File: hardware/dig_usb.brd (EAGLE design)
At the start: 146.1 x 102.6 mm, 175 parts, among them IC101 AT90USB1287-AU, IC102 74HC166D, IC103 MAX487CSA, IC202 DS1337S, IC301 LTV-356T, IC302 LTV-356T, IC303 LTV-356T, IC304 LTV-356T, IC305 LTV-356T, IC306 LTV-356T, IC307 LTV-356T, IC308 LTV-356T, K401 S202S02, K402 S202S02, K403 S202S02, K404 S202S02, K405 S202S02, K406 S202S02, K407 S202S02, K408 S202S02, Q1 16MHz, Q201 32,768kHz, T301 BCR191, T302 BCR191, T303 BCR191, T304 BCR191, T305 BCR191, T306 BCR191, T307 BCR191, T308 BCR191, X102 ISP, X301 RIA-73-02, X302 RIA-73-02, X303 RIA-73-02, X304 RIA-73-02, X305 RIA-73-02, X401 RIA-73-02, X402 RIA-73-02, X403 RIA-73-02, X404 RIA-73-02, X405 RIA-73-02, X406 RIA-73-02, X407 RIA-73-02

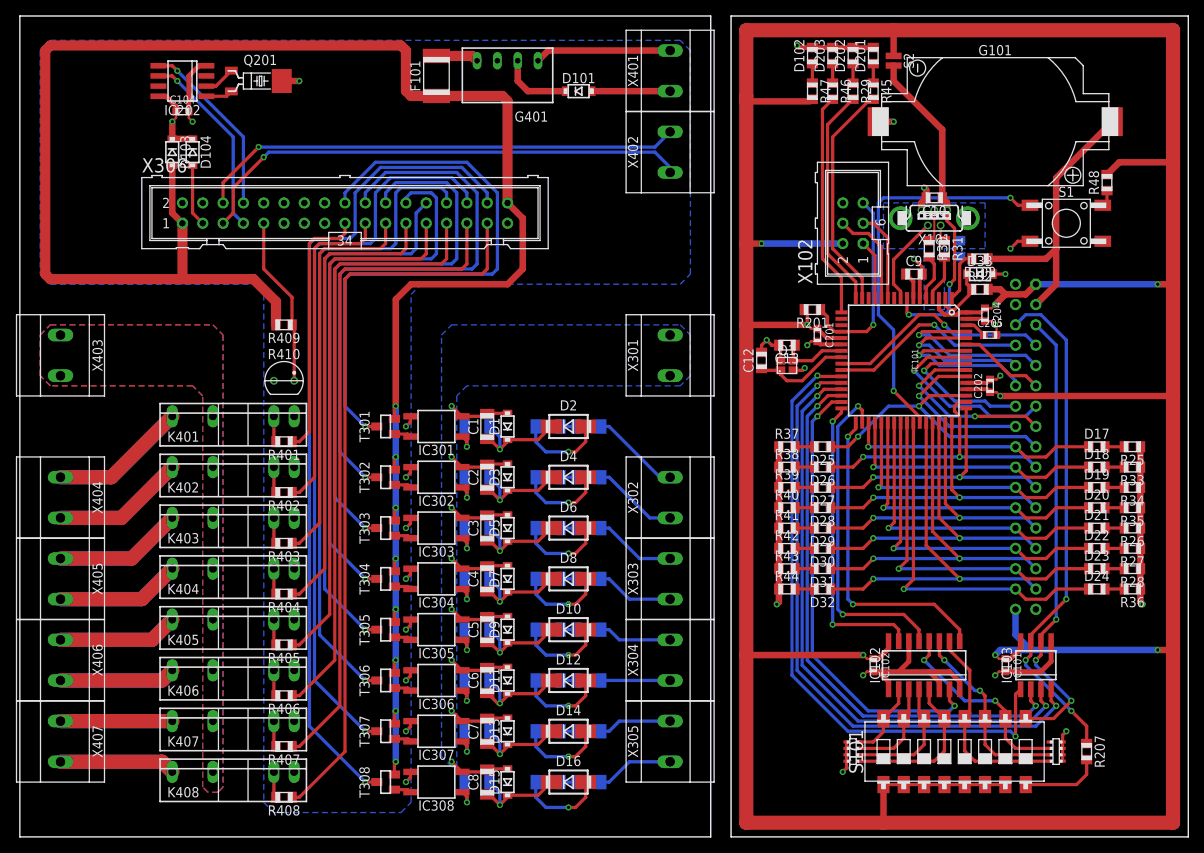
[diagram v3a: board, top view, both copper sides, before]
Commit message: Steckbare Anschlüsse zu dig_usb hinzugefügt
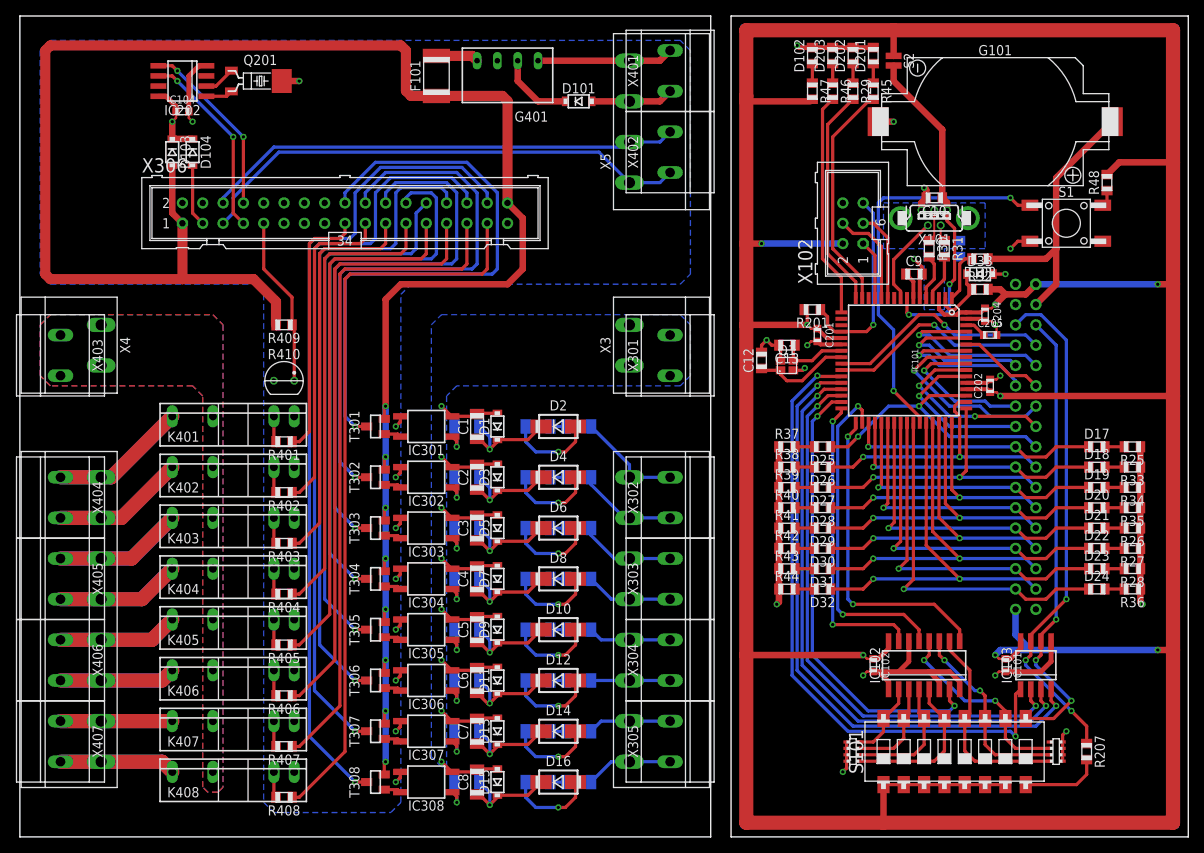
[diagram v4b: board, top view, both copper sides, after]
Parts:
- added X1, X2: AKL_249-08, anschluss:AKL_230-08
- added X3, X4: AKL_230-02, anschluss:AKL_230-02
- added X5: AKL_230-04, anschluss:AKL_230-04
- moved R1 1.27 mm to (64.8, 50.8)
- moved R10 1.27 mm to (64.8, 31.8)
- moved R11 1.27 mm to (69.8, 31.8)
- moved R13 1.27 mm to (64.8, 25.4)
- moved R14 1.27 mm to (69.8, 25.4)
- moved R16 1.27 mm to (64.8, 19.1)
- moved R17 1.27 mm to (69.8, 19.1)
- moved R19 1.27 mm to (64.8, 12.7)
- moved R2 1.27 mm to (69.8, 50.8)
- moved R20 1.27 mm to (69.8, 12.7)
- moved R22 1.27 mm to (64.8, 6.35)
- moved R23 1.27 mm to (69.8, 6.35)
- moved R4 1.27 mm to (64.8, 44.5)
- moved R5 1.27 mm to (69.8, 44.5)
- moved R7 1.27 mm to (64.8, 38.1)
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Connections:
- net GNDIO: now also X3.P$1, X3.P$2
- net L: now also X4.P$1, X4.P$2
- net N$133: now also X5.P$2
- net N$134: now also X5.P$1
- net N$19: now also X5.P$4
- net N$24: now also X5.P$3
- net N$45: now also X2.P$7
- net N$46: now also X2.P$8
- net N$47: now also X2.P$5
- net N$48: now also X2.P$6
- net N$56: now also X2.P$4
- net N$58: now also X2.P$3
- net N$59: now also X2.P$1
- net N$60: now also X2.P$2
- net N$68: now also X1.P$1
- net N$72: now also X1.P$2
- net N$74: now also X1.P$3
- net N$76: now also X1.P$4
- net N$78: now also X1.P$5
- net N$82: now also X1.P$6
- net N$84: now also X1.P$7
- net N$89: now also X1.P$8
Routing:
- net N$46: track 11.2 -> 13.4 mm
- net N$45: track 10.7 -> 12.5 mm
- net N$48: track 10.2 -> 12.0 mm
- net +5V: track 736.5 -> 737.7 mm
- net N$60: track 9.14 -> 10.4 mm
- net N$56: track 9.14 -> 10.4 mm
- net N$47: track 9.66 -> 10.9 mm
- net N$59: track 9.66 -> 10.9 mm
- net N$58: track 8.61 -> 9.88 mm
- net N$133: track 61.1 -> 59.9 mm, vias 1 -> 0
- net N$97: track 68.5 -> 67.9 mm
- net N$96: track 70.6 -> 70.1 mm
- net N$95: track 72.1 -> 71.5 mm
- net N$94: track 73.5 -> 73.0 mm
- net N$101: track 103.4 -> 102.8 mm
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
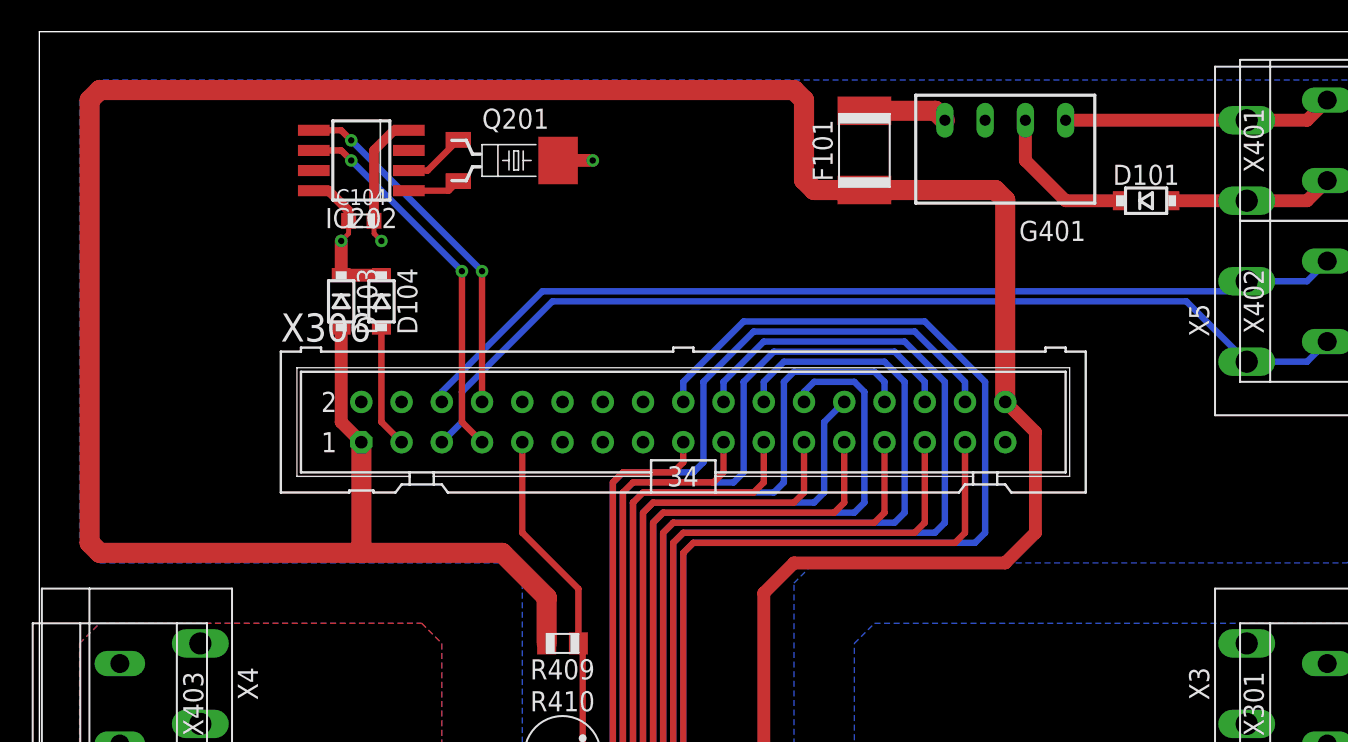
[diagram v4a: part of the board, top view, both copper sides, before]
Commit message: RJ45 Buchsen für Bus an dig_usb
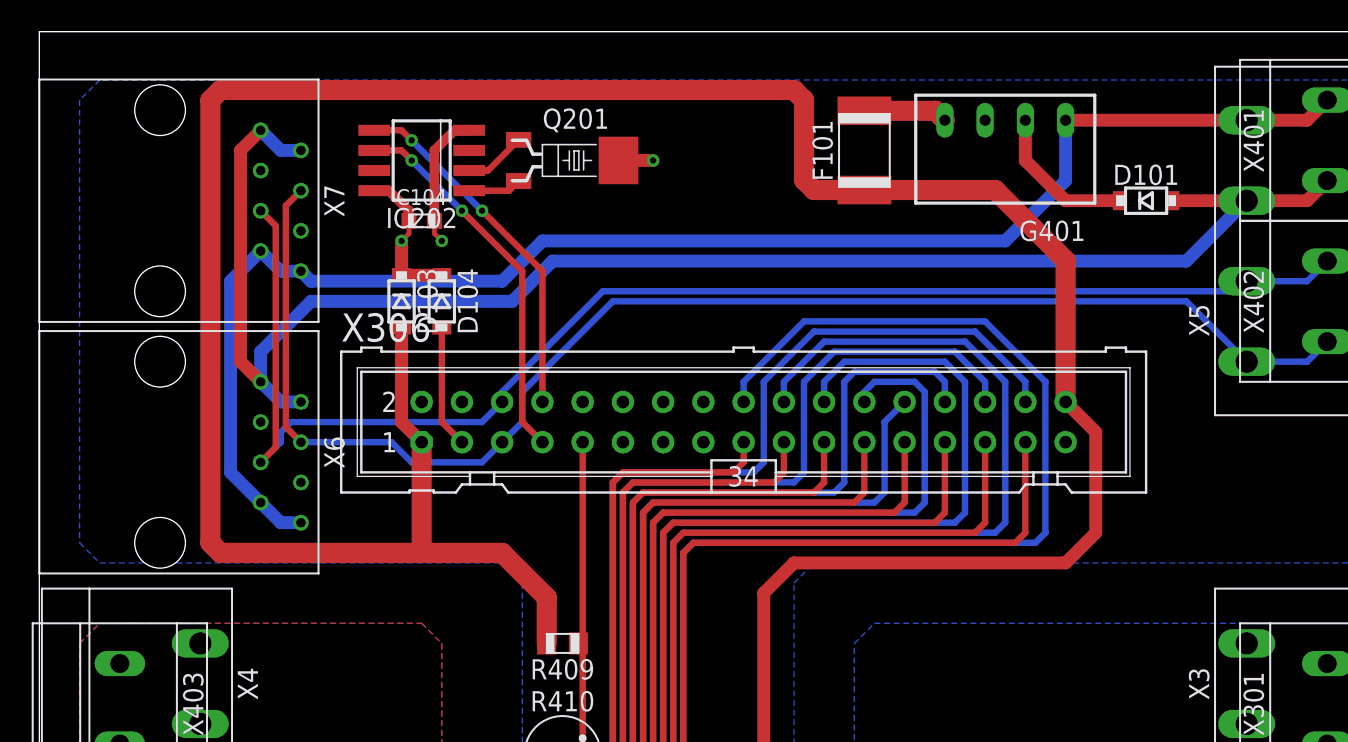
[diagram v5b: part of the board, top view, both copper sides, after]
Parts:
- added X6, X7: (no value), stecker:C-BMJ-0102
- moved X306 3.81 mm to (44.5, 77.5)
- moved C104 3.81 mm to (24.1, 90.2)
- moved D103 3.81 mm to (22.9, 85.1)
- moved D104 3.81 mm to (25.4, 85.1)
- moved IC202 3.81 mm to (24.1, 94.0)
- moved Q201 3.81 mm to (31.8, 94.0)
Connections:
- removed net N$19: G401.1, X401.2, X5.P$4
- removed net N$24: D101.A, X401.1, X5.P$3
- new net V+: D101.A, X401.1, X5.P$3, X6.P$1, X6.P$2, X7.P$1, X7.P$2
- new net V-: G401.1, X401.2, X5.P$4, X6.P$7, X6.P$8, X7.P$7, X7.P$8
- net N$133: now also X6.P$5, X7.P$5
- net N$134: now also X6.P$4, X7.P$4
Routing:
- net V+: track 0.00 -> 101.4 mm
- net V-: track 0.00 -> 95.6 mm
- net N$133: track 59.9 -> 90.0 mm
- net N$134: track 62.8 -> 89.4 mm
- net N$19: track 17.0 -> 0.00 mm
- net N$24: track 10.3 -> 0.00 mm
- net +5V: track 737.7 -> 727.9 mm
- net N$99: track 81.2 -> 85.0 mm
- net N$97: track 67.9 -> 71.8 mm
- net N$95: track 71.5 -> 75.3 mm
- net N$93: track 92.1 -> 95.9 mm
- net N$92: track 83.5 -> 87.4 mm
- net N$90: track 66.5 -> 70.3 mm
- net N$88: track 58.0 -> 61.8 mm
- net N$87: track 49.5 -> 53.3 mm
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
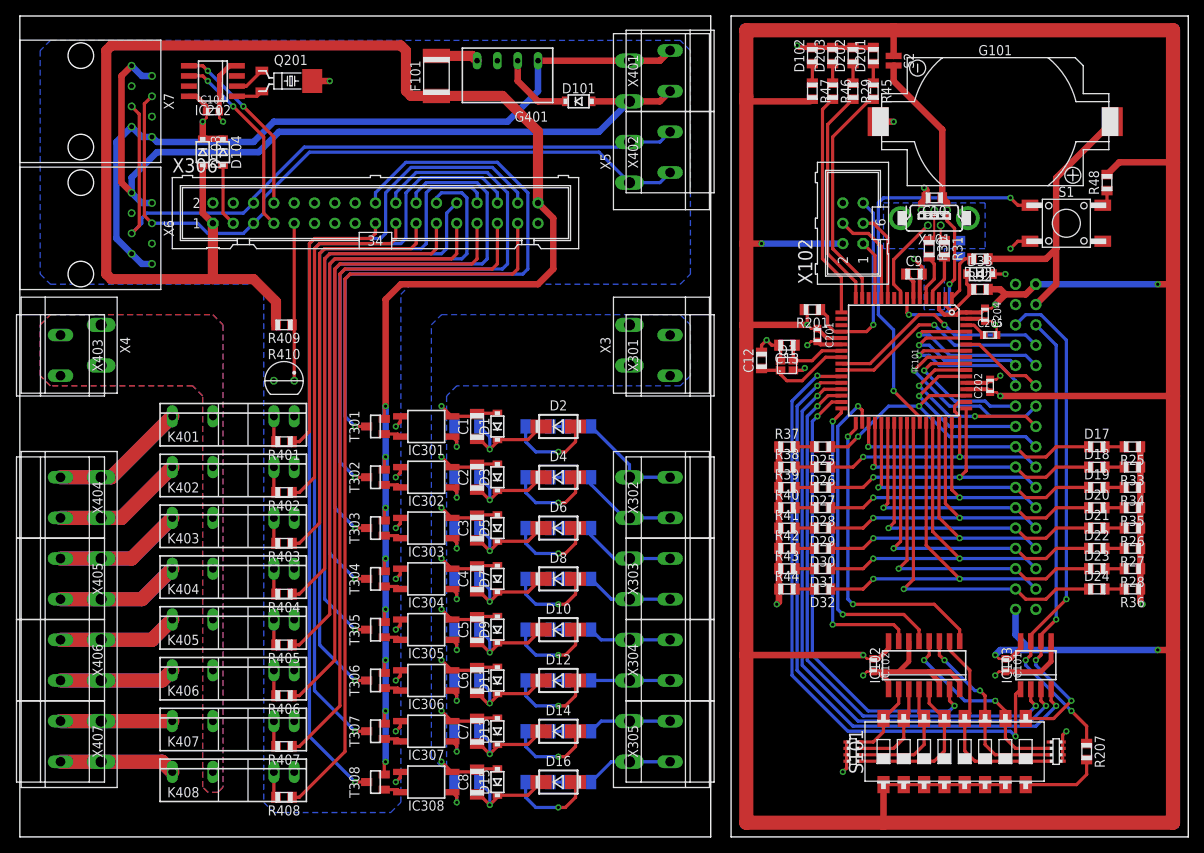
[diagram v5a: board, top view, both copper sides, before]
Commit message: Routing auf dig_usb verfeinert
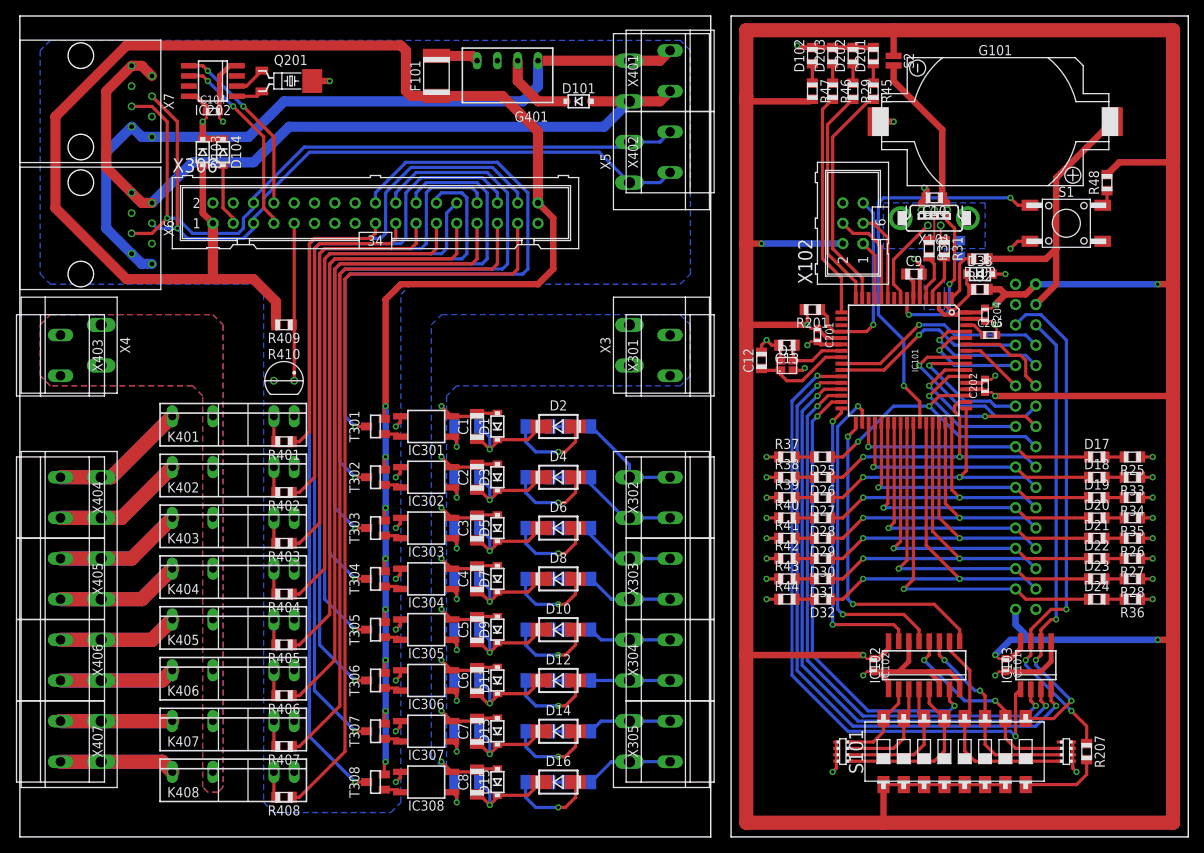
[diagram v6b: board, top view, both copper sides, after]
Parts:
- moved R209 1.27 mm to (130.8, 10.2)
- moved D19 1.27 mm to (134.6, 41.9)
- moved D20 1.27 mm to (134.6, 39.4)
- moved D21 1.27 mm to (134.6, 36.8)
- moved D22 1.27 mm to (134.6, 34.3)
- moved D23 1.27 mm to (134.6, 31.8)
- moved D27 1.27 mm to (100.3, 41.9)
- moved D28 1.27 mm to (100.3, 39.4)
- moved D29 1.27 mm to (100.3, 36.8)
- moved D30 1.27 mm to (100.3, 34.3)
- moved D31 1.27 mm to (100.3, 31.8)
- moved R26 1.27 mm to (139.1, 36.8)
- moved R27 1.27 mm to (139.1, 34.3)
- moved R28 1.27 mm to (139.1, 31.8)
- moved R34 1.27 mm to (139.1, 41.9)
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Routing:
- net GND: track 150.3 -> 134.7 mm, vias 27 -> 41
- net N$138: track 20.1 -> 7.98 mm, vias 1 -> 0
- net N$136: track 19.4 -> 14.3 mm
- net N$135: track 22.3 -> 17.2 mm
- net N$133: track 90.0 -> 92.9 mm, vias 0 -> 1
- net N$141: track 23.4 -> 20.9 mm
- net N$142: track 20.6 -> 18.0 mm
- net +5V: track 727.9 -> 730.2 mm
- net N$134: track 89.4 -> 91.4 mm, vias 0 -> 1
- net V+: track 101.4 -> 103.0 mm
- net N$140: track 18.9 -> 17.6 mm
- net N$29: track 19.7 -> 20.9 mm
- net N$28: track 15.8 -> 17.1 mm
- net N$27: track 12.5 -> 13.7 mm
- net N$26: track 9.65 -> 10.9 mm
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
